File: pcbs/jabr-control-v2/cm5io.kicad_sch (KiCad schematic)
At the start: 21 parts, among them J10001 ARJM11D7-502-AB-EW2, J10002 TYPE-C-31-M-12, J1001 48406-0003, J1002 FH12-22S-0.5SH, U1001 AP22653FDZ-7, U1002 PESD4USB3BTTS-QX, U1003 PESD4USB3BTTS-QX, U1004 PESD4USB3BTTS-QX, U1005 PESD4USB3BTTS-QX, U2401 PESD4USB3BTTS-QX, U2402 PESD4USB3BTTS-QX

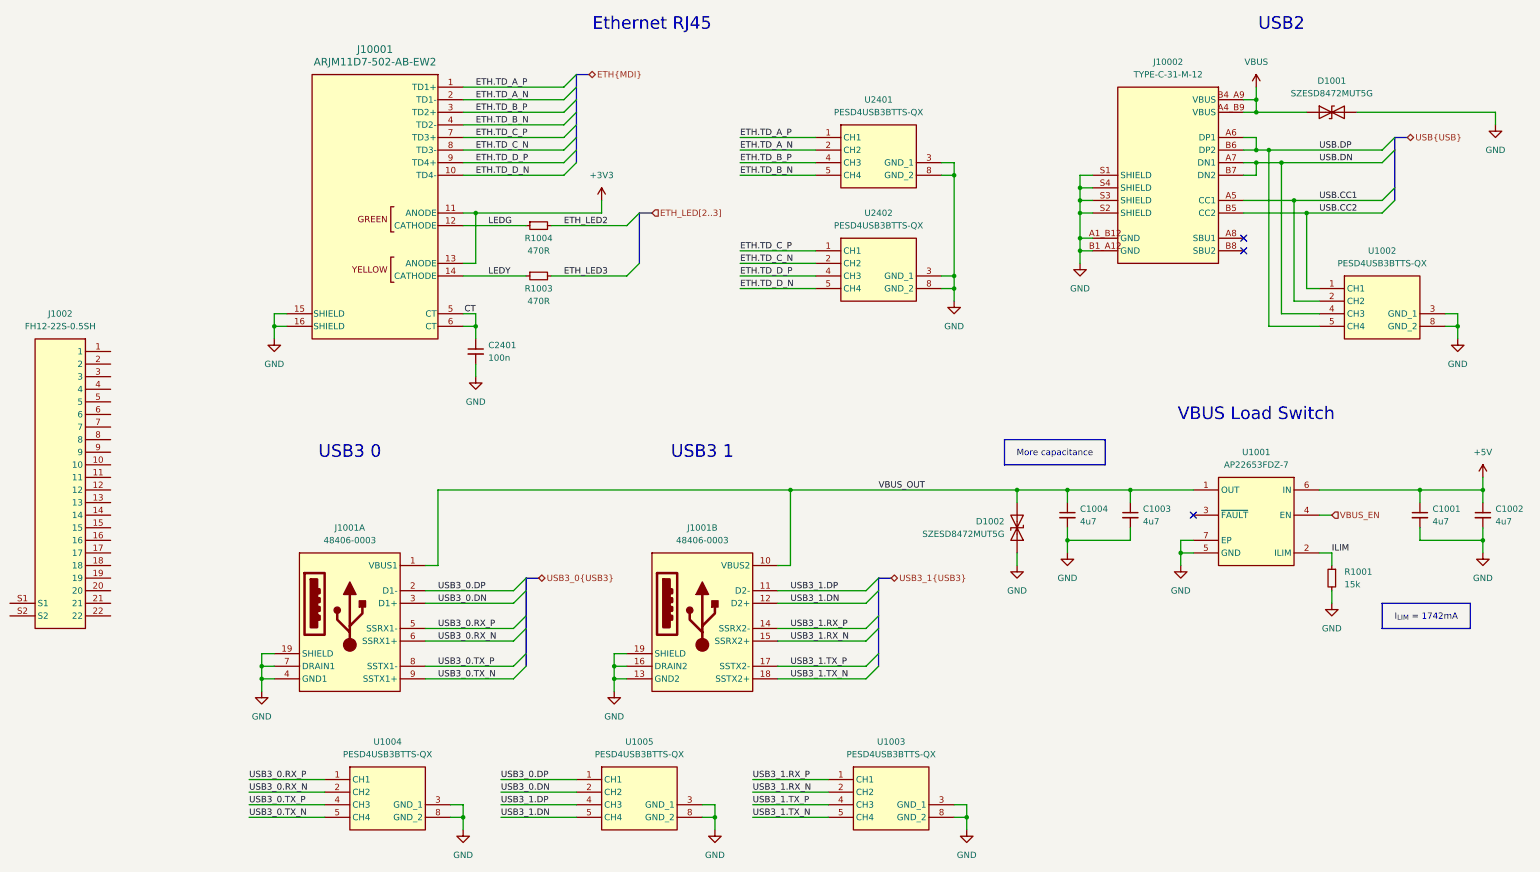
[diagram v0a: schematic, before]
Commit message: PCI11010C Schematic sheet mostly done
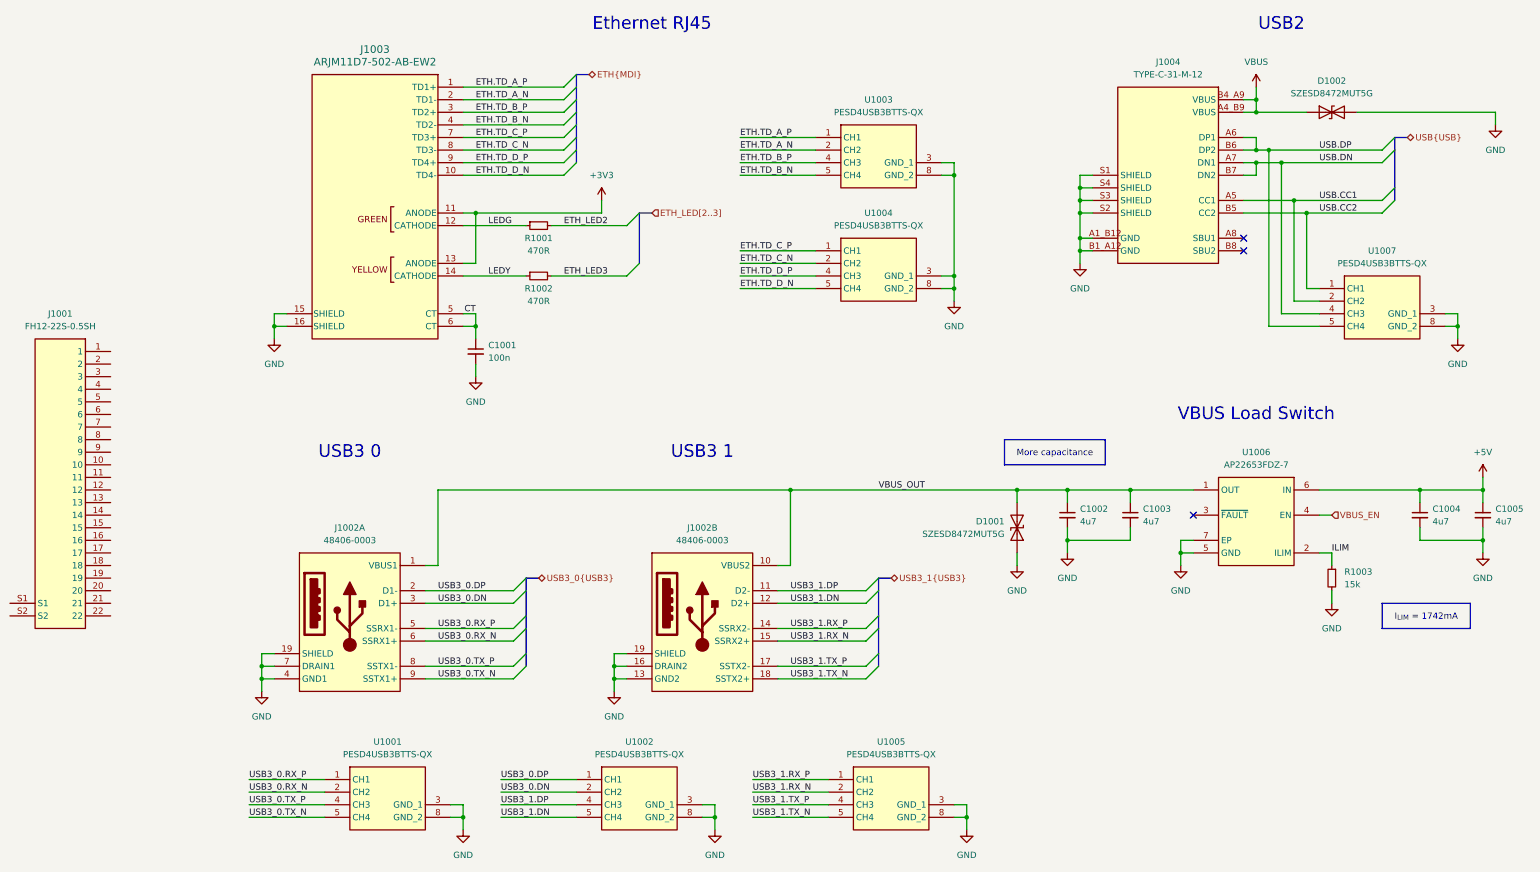
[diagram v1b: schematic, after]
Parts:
- renumbered C2401 to C1001, C1004 to C1002, C1001 to C1004, C1002 to C1005, D1002 to D1001, D1001 to D1002, J1002 to J1001, J1001 to J1002, J10001 to J1003, J10002 to J1004, R1004 to R1001, R1003 to R1002, R1001 to R1003, U1004 to U1001, U1005 to U1002, U2401 to U1003, U2402 to U1004, U1003 to U1005, U1001 to U1006, U1002 to U1007

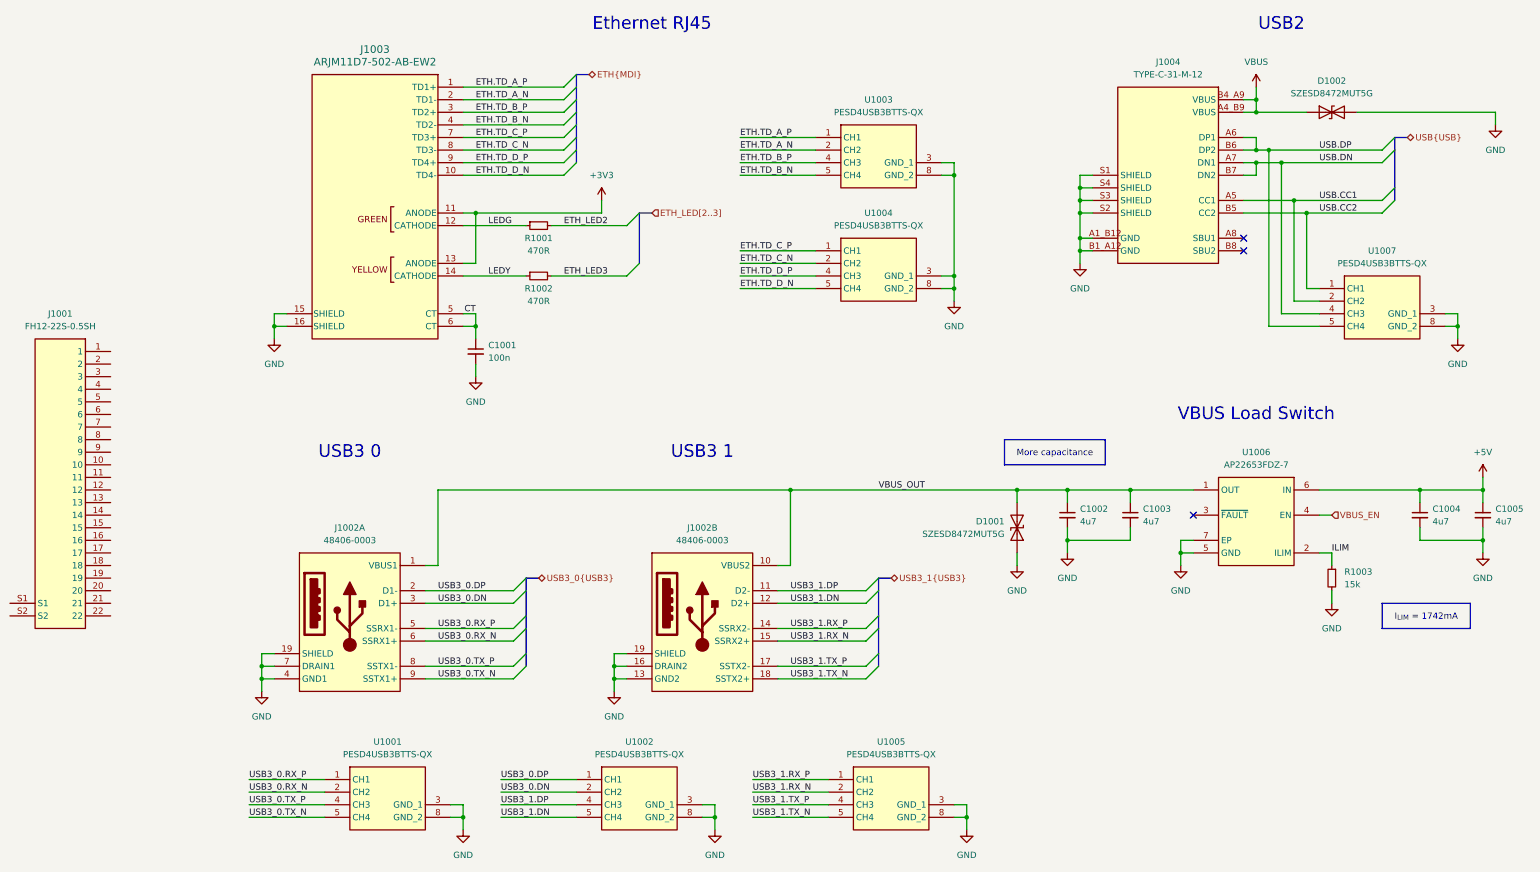
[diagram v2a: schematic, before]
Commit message: Removed power button reset to switch (power will be cycled anyway)
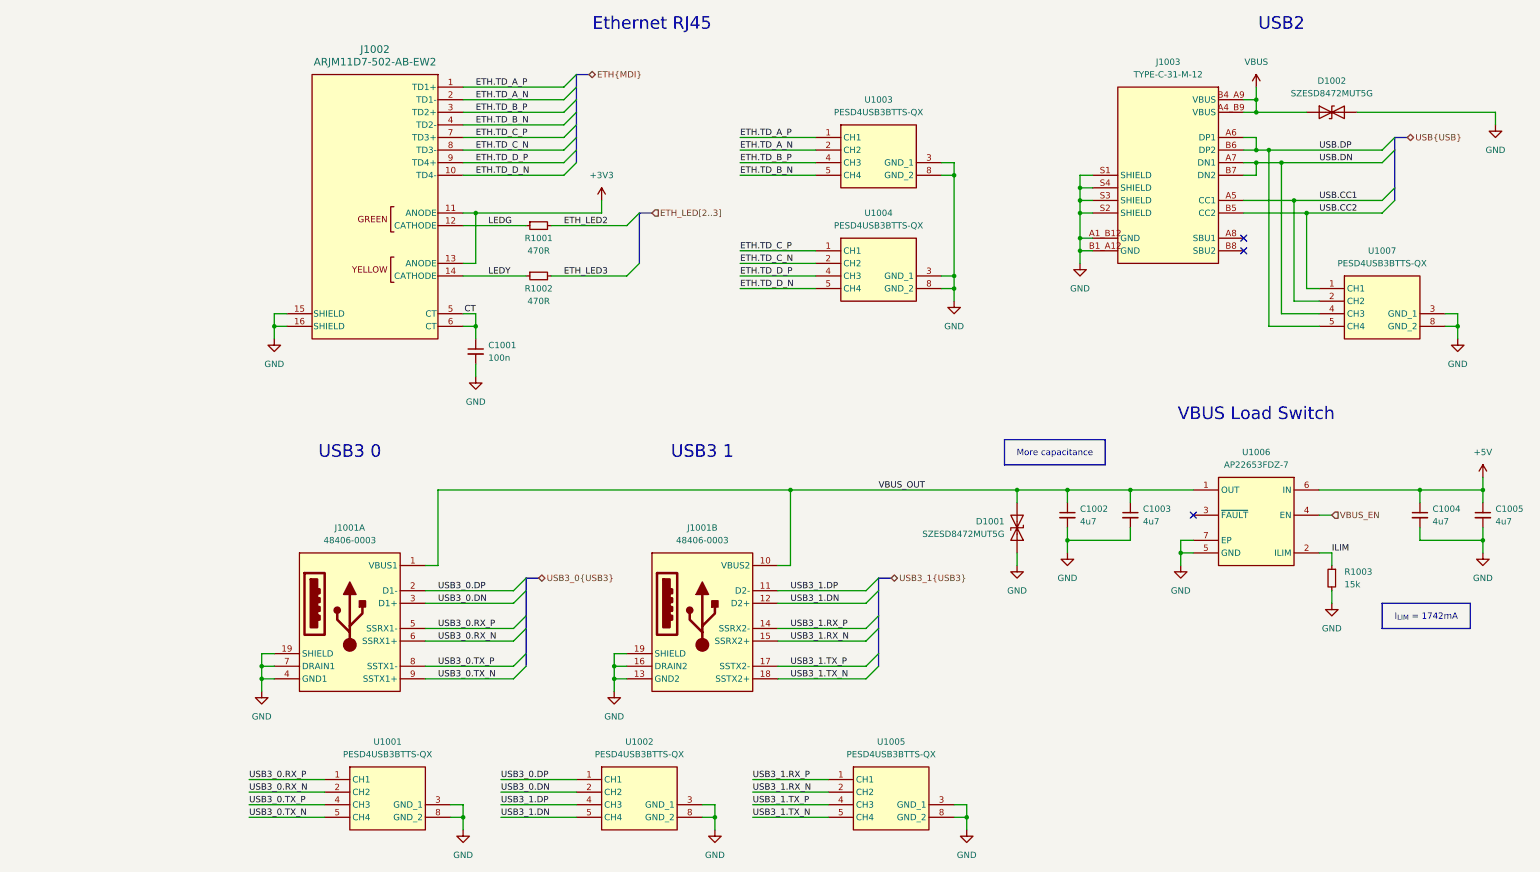
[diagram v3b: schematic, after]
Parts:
- removed J1001: FH12-22S-0.5SH, project_footprints:Hirose_FH12-22S-0.5SH_1x22-1MP_P0.50mm_Horizontal, symbol CONN-FPC:FH12-22S-0.5SH
- renumbered J1002 to J1001, J1003 to J1002, J1004 to J1003
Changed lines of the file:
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@@
-	)
-	(symbol
-		(lib_id "CONN-FPC:FH12-22S-0.5SH")
-		(at -17.78 88.9 0)
-		(mirror y)
-		(unit 1)
-		(body_style 1)
-		(exclude_from_sim no)
-		(in_bom yes)
-		(on_board yes)
-		(in_pos_files yes)
-		(dnp no)
-		(fields_autoplaced yes)
-		(property "Reference" "J1001"
-			(at -17.78 83.82 0)
-			(show_name no)
-			(do_not_autoplace no)
-			(effects
-				(font
-					(size 1.27 1.27)
-				)
-			)
-		)
-		(property "Value" "FH12-22S-0.5SH"
-			(at -17.78 86.36 0)
-			(show_name no)
-			(do_not_autoplace no)
-			(effects
-				(font
-					(size 1.27 1.27)
-				)
-			)
-		)
-		(property "Footprint" "project_footprints:Hirose_FH12-22S-0.5SH_1x22-1MP_P0.50mm_Horizontal"
-			(at -19.05 152.4 0)
-			(hide yes)
-			(show_name no)
-			(do_not_autoplace no)
-			(effects
-				(font
-					(size 1.27 1.27)
-				)
-			)
-		)
-		(property "Datasheet" "https://www.mouser.co.uk/datasheet/3/731/1/FH12_22S_0.5SH_55_CL0586_0532_7_55_2DDrawing_0000987484.pdf"
-			(at -17.78 149.86 0)
-			(hide yes)
-			(show_name no)
-			(do_not_autoplace no)
-			(effects
-				(font
-					(size 1.27 1.27)
-				)
-			)
-		)
-		(property "Description" ""
-			(at -17.78 88.9 0)
-			(hide yes)
-			(show_name no)
-			(do_not_autoplace no)
-			(effects
-				(font
-					(size 1.27 1.27)
-				)
-			)
-		)
-		(property "Field6" ""
-			(at -17.78 88.9 0)
-			(hide yes)
-			(show_name no)
-			(do_not_autoplace no)
-			(effects
-				(font
-					(size 1.27 1.27)
-				)
-			)
-		)
-		(property "Field7" ""
-			(at -17.78 88.9 0)
-			(hide yes)
-			(show_name no)
-			(do_not_autoplace no)
-			(effects
-				(font
-					(size 1.27 1.27)
-				)
-			)
-		)
-		(property "Part Description" ""
-			(at -17.78 88.9 0)
-			(hide yes)
-			(show_name no)
-			(do_not_autoplace no)
-			(effects
-				(font
-					(size 1.27 1.27)
-				)
-			)
-		)
-		(pin "7"
-		)
-		(pin "22"
-		)
-		(pin "4"
-		)
-		(pin "2"
-		)
-		(pin "15"
-		)
-		(pin "S2"
-		)
-		(pin "12"
-		)
-		(pin "6"
-		)
-		(pin "1"
-		)
-		(pin "9"
-		)
-		(pin "16"
-		)
-		(pin "14"
-		)
-		(pin "17"
-		)
-		(pin "13"
-		)
-		(pin "3"
-		)
-		(pin "5"
-		)
-		(pin "8"
-		)
-		(pin "18"
-		)
-		(pin "11"
-		)
-		(pin "19"
-		)
-		(pin "20"
-		)
-		(pin "21"
-		)
-		(pin "10"
-		)
-		(pin "S1"
-		)
-		(instances
-			(project "jabr-control-v2"
-				(path "/f91ec272-d09a-4038-bbbb-962739a92c51/adc0b005-3094-4656-96e7-4ee9fb2ab719"
-					(reference "J1001")
-					(unit 1)
-				)
-			)
-		)
 	)
 	(symbol
@@
 		(in_pos_files yes)
 		(dnp no)
-		(property "Reference" "J1004"
+		(property "Reference" "J1003"
 			(at 205.74 33.02 0)
 			(show_name no)
@@
 			(project "jabr-control-v2"
 				(path "/f91ec272-d09a-4038-bbbb-962739a92c51/adc0b005-3094-4656-96e7-4ee9fb2ab719"
-					(reference "J1004")
+					(reference "J1003")
 					(unit 1)
 				)
@@
 		(dnp no)
 		(fields_autoplaced yes)
-		(property "Reference" "J1003"
+		(property "Reference" "J1002"
 			(at 45.72 30.48 0)
 			(show_name no)
@@
 			(project "jabr-control-v2"
 				(path "/f91ec272-d09a-4038-bbbb-962739a92c51/adc0b005-3094-4656-96e7-4ee9fb2ab719"
-					(reference "J1003")
+					(reference "J1002")
 					(unit 1)
 				)
@@
 		(dnp no)
 		(fields_autoplaced yes)
-		(property "Reference" "J1002"
+		(property "Reference" "J1001"
 			(at 40.64 127 0)
 			(show_name no)
@@
 			(project "jabr-control-v2"
 				(path "/f91ec272-d09a-4038-bbbb-962739a92c51/adc0b005-3094-4656-96e7-4ee9fb2ab719"
-					(reference "J1002")
+					(reference "J1001")
 					(unit 1)
 				)
@@
 		(dnp no)
 		(fields_autoplaced yes)
-		(property "Reference" "J1002"
+		(property "Reference" "J1001"
 			(at 111.76 127 0)
 			(show_name no)
@@
 			(project "jabr-control-v2"
 				(path "/f91ec272-d09a-4038-bbbb-962739a92c51/adc0b005-3094-4656-96e7-4ee9fb2ab719"
-					(reference "J1002")
+					(reference "J1001")
 					(unit 2)
 				)

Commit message: Schematic done
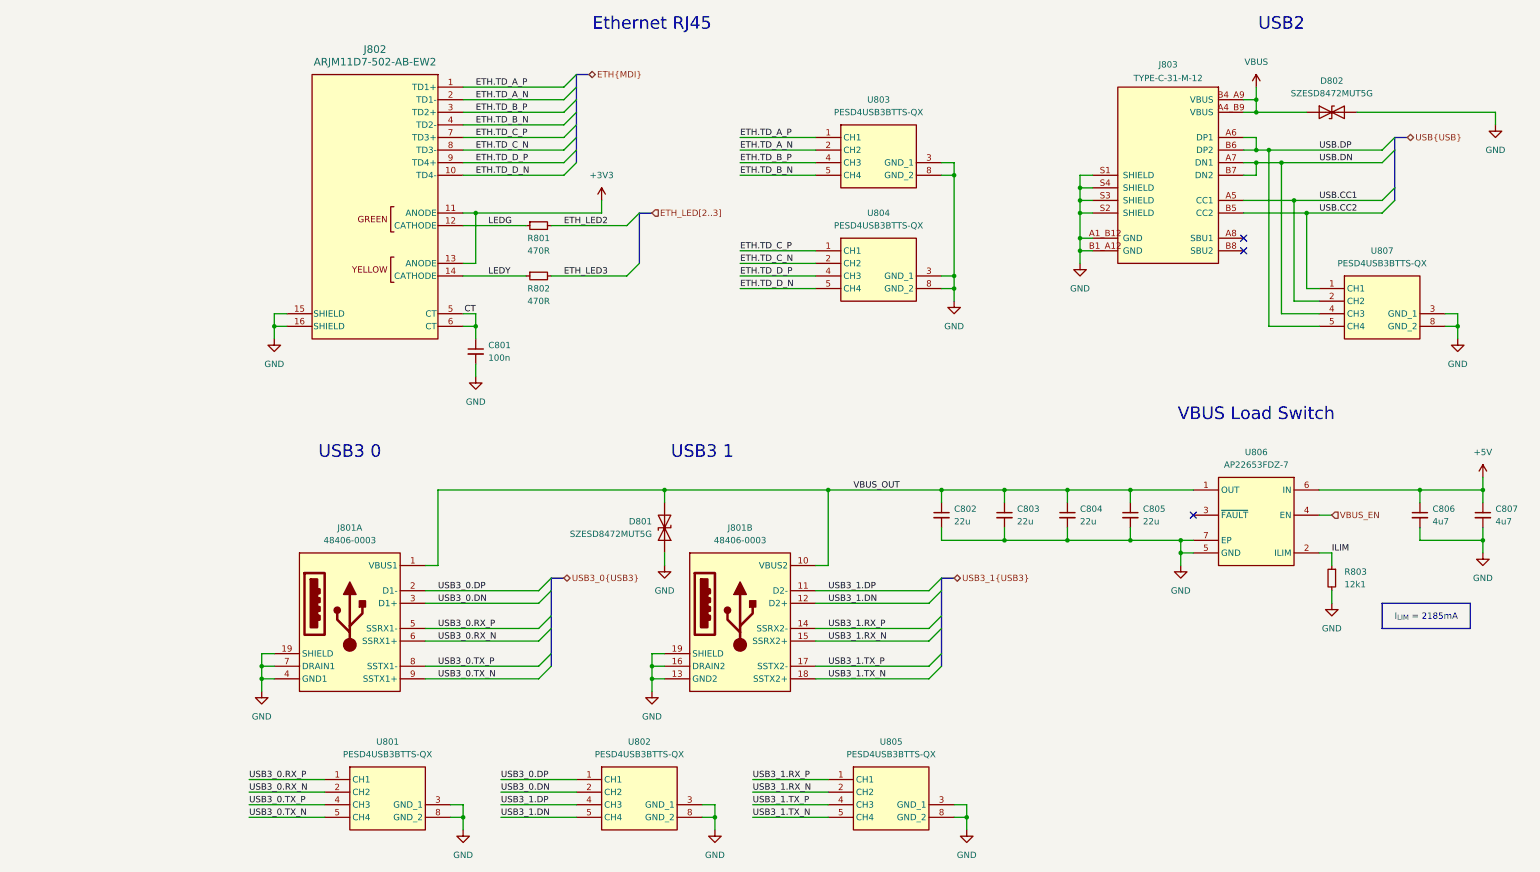
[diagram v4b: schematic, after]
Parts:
- removed C1002, C1003: 4u7, project_footprints:C_0402, symbol DEV:C_SMALL
- removed J1003: TYPE-C-31-M-12, project_footprints:TYPE-C-31-M-12, symbol USB-CONN:TYPE-C-31-M-12
- added C802, C803, C804, C805: 22u, project_footprints:C_0805, symbol DEV:C_SMALL
- added J803: TYPE-C-31-M-12, project_footprints:TYPE-C-31-M-12, symbol USB-CONN:TYPE-C-31-M-12
- R801: renamed from R1001; footprint (none) -> project_footprints:R_0402
- R802: renamed from R1002; footprint (none) -> project_footprints:R_0402
- R803: renamed from R1003; value 15k -> 12k1; footprint (none) -> project_footprints:R_0402
- renumbered C1001 to C801, C1004 to C806, C1005 to C807, D1001 to D801, D1002 to D802, J1001 to J801, J1002 to J802, U1001 to U801, U1002 to U802, U1003 to U803, U1004 to U804, U1005 to U805, U1006 to U806, U1007 to U807
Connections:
- net GND: now also C802.2, C803.2, C804.2, C805.2, J803.A1_B12 (GND), J803.B1_A12 (GND), J803.S1 (SHIELD), J803.S2 (SHIELD), J803.S3 (SHIELD), J803.S4 (SHIELD)
- net USB.CC1: now also J803.A5 (CC1)
- net USB.CC2: now also J803.B5 (CC2)
- net USB.DN: now also J803.A7 (DN1), J803.B7 (DN2)
- net USB.DP: now also J803.A6 (DP1), J803.B6 (DP2)
- net VBUS: now also J803.A4_B9 (VBUS), J803.B4_A9 (VBUS)
- net VBUS_OUT: now also C802.1, C803.1, C804.1, C805.1
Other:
- moved on the sheet: D801, J801B
